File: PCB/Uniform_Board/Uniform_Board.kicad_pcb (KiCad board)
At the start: 2 copper layers, 301.5 x 93.4 mm, 167 parts, among them J1 PCIE_x1_SAMTEC_PCIE-036-02-F-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, M1 MountingHole_2.7mm_M2.5, M10 MountingHole_2.7mm_M2.5, M2 MountingHole_2.7mm_M2.5, M3 MountingHole_2.7mm_M2.5, M4 MountingHole_2.7mm_M2.5, M5 MountingHole_2.7mm_M2.5, M6 MountingHole_2.7mm_M2.5, M7 MountingHole_2.7mm_M2.5, M8 MountingHole_2.7mm_M2.5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

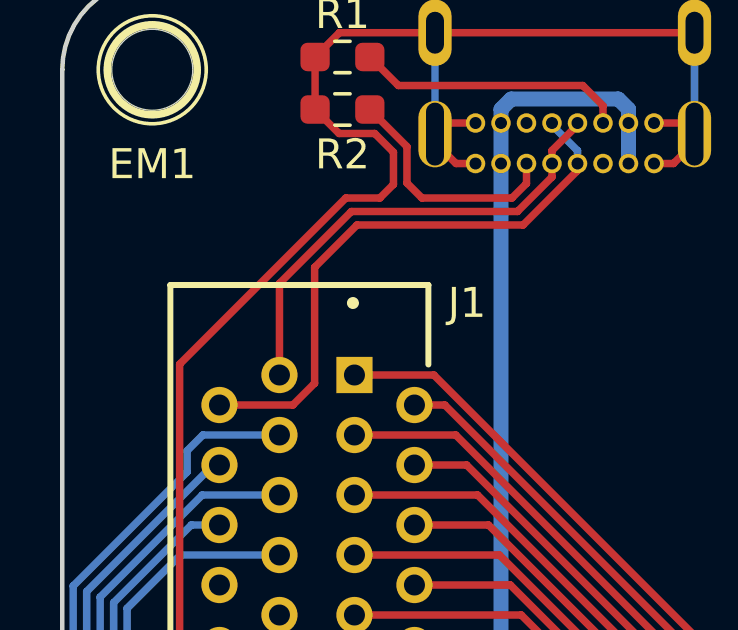
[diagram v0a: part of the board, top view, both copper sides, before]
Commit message: Uniform module traces first pass complete
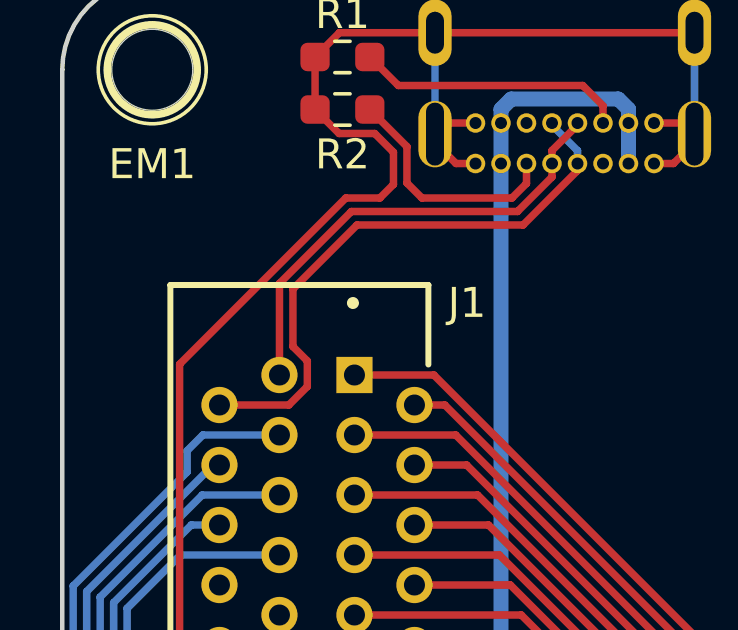
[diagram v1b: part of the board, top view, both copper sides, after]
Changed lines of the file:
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@@
   (segment (start 56.1 111.825) (end 56.1 111.393548) (width 0.25) (layer "F.Cu") (net 91))
   (segment (start 56.95 112.061435) (end 55.137394 113.87404) (width 0.25) (layer "F.Cu") (net 92))
-  (segment (start 48.1875 119.15) (end 47.4625 119.875) (width 0.25) (layer "F.Cu") (net 92))
-  (segment (start 49.599178 113.87404) (end 48.1875 115.285718) (width 0.25) (layer "F.Cu") (net 92))
-  (segment (start 48.1875 115.285718) (end 48.1875 119.15) (width 0.25) (layer "F.Cu") (net 92))
-  (segment (start 47.4625 119.875) (end 45.015 119.875) (width 0.25) (layer "F.Cu") (net 92))
+  (segment (start 47.46452 117.92702) (end 47.943511 118.406011) (width 0.25) (layer "F.Cu") (net 92))
+  (segment (start 47.328114 119.875) (end 45.015 119.875) (width 0.25) (layer "F.Cu") (net 92))
+  (segment (start 49.599178 113.87404) (end 47.46452 116.008698) (width 0.25) (layer "F.Cu") (net 92))
+  (segment (start 47.46452 116.008698) (end 47.46452 117.92702) (width 0.25) (layer "F.Cu") (net 92))
+  (segment (start 56.95 111.825) (end 56.95 112.061435) (width 0.25) (layer "F.Cu") (net 92))
+  (segment (start 47.943511 118.406011) (end 47.943511 119.259603) (width 0.25) (layer "F.Cu") (net 92))
+  (segment (start 47.943511 119.259603) (end 47.328114 119.875) (width 0.25) (layer "F.Cu") (net 92))
   (segment (start 55.137394 113.87404) (end 49.599178 113.87404) (width 0.25) (layer "F.Cu") (net 92))
-  (segment (start 56.95 111.825) (end 56.95 112.061435) (width 0.25) (layer "F.Cu") (net 92))
   (segment (start 56.1 110.543548) (end 56.1 110.475) (width 0.25) (layer "B.Cu") (net 92))
   (segment (start 56.95 111.825) (end 56.95 111.393548) (width 0.25) (layer "B.Cu") (net 92))
